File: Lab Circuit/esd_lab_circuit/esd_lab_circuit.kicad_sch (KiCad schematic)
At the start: 5 parts, among them U3 74LS373, U5 ATF16V8Bxx-xxPU, U6 M48Z35

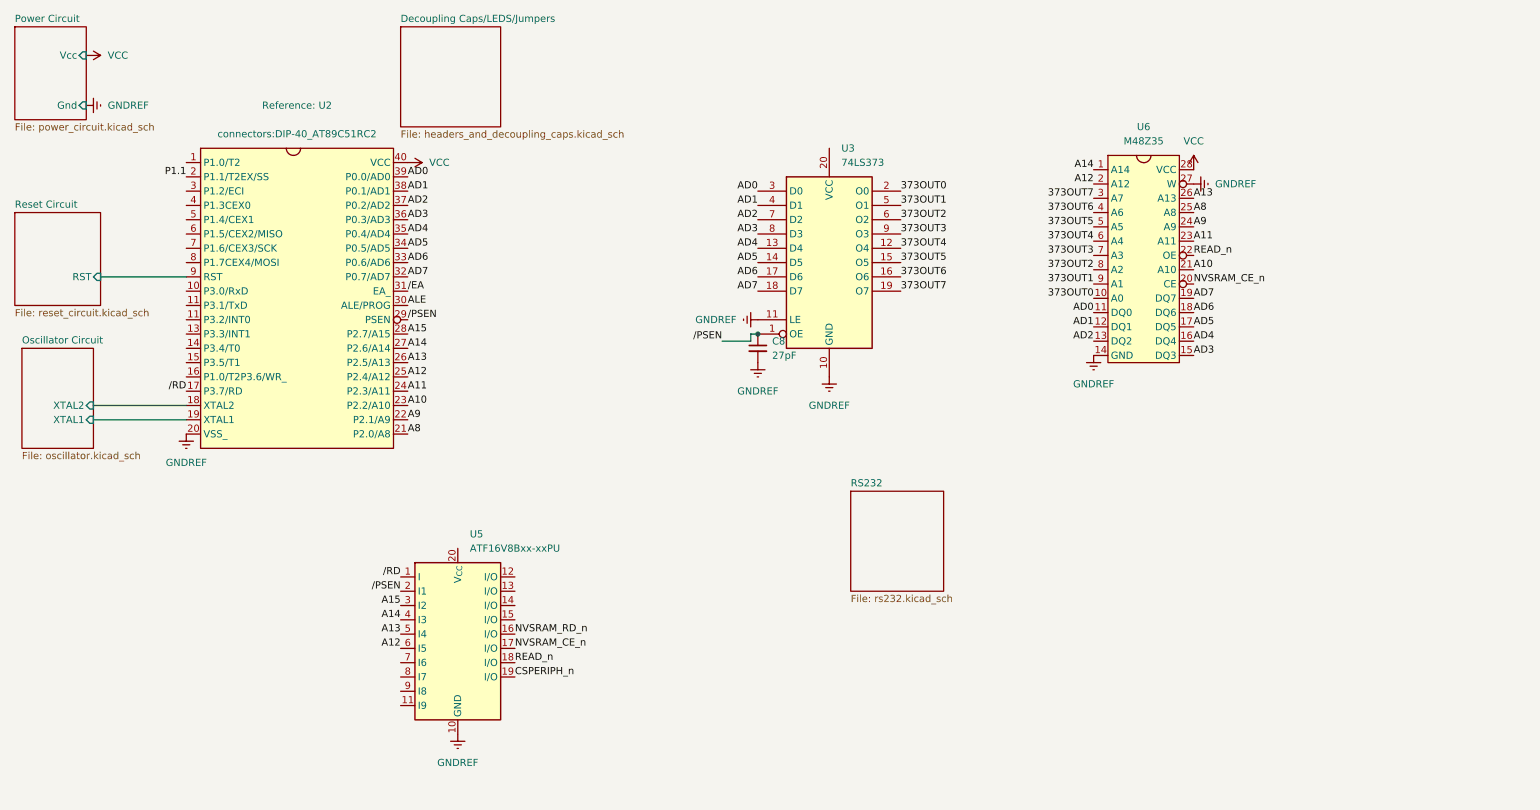
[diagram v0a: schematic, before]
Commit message: Added Debug Latch to schematic
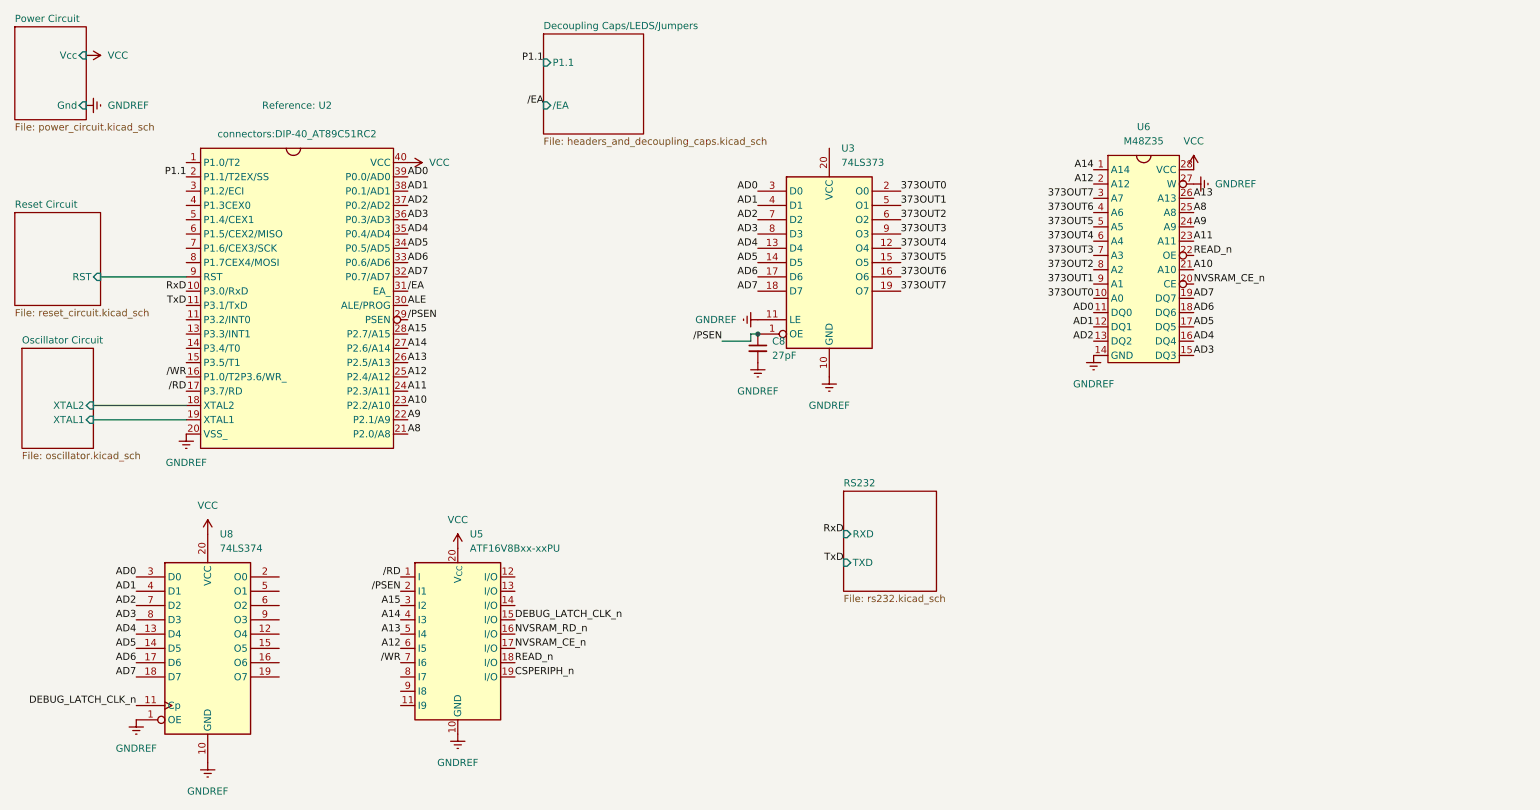
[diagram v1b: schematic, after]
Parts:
- added U8: 74LS374, symbol ESD:74LS374
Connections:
- net AD0: now also U8.3 (D0)
- net AD1: now also U8.4 (D1)
- net AD2: now also U8.7 (D2)
- net AD3: now also U8.8 (D3)
- net AD4: now also U8.13 (D4)
- net AD5: now also U8.14 (D5)
- net AD6: now also U8.17 (D6)
- net AD7: now also U8.18 (D7)
- net GNDREF: now also U8.1 (OE), U8.10 (GND)
- net VCC: now also U5.20 (V_{CC}), U8.20 (VCC)
- net DEBUG_LATCH_CLK_n: now reaches U5.15 (I/O)
- net DEBUG_LATCH_CLK_n: now also U8.11 (Cp)
- net /WR: now reaches U5.7 (I6)
- net /WR: now also U2.16 (P1.0/T2P3.6/WR_)
- net RxD: now reaches U2.10 (P3.0/RxD)
- net TxD: now reaches U2.11 (P3.2/INT0)
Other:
- sheet Decoupling Caps/LEDS/Jumpers ports: added P1.1, /EA; removed none
- sheet RS232 ports: added RXD, TXD; removed none

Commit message: Got to the point where lab 3 part 1 step 3 is done
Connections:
- net GNDREF: no longer U6.27 (W)
- net NVSRAM_WR_n: now reaches U5.14 (I/O)
- net NVSRAM_WR_n: now also U6.27 (W)
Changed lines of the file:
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@@
+		)
+	)
+	(label "NVSRAM_WR_n"
+		(at 102.87 118.11 0)
+		(effects
+			(font
+				(size 1.27 1.27)
+			)
+			(justify left bottom)
 		)
 	)
@@
 	(label "{slash}EA"
 		(at 83.82 62.23 0)
+		(effects
+			(font
+				(size 1.27 1.27)
+			)
+			(justify left bottom)
+		)
+	)
+	(label "NVSRAM_WR_n"
+		(at 223.52 43.18 0)
 		(effects
 			(font
@@
 					(unit 1)
 				)
-			)
-		)
-	)
-	(symbol
-		(lib_id "power:GNDREF")
-		(at 223.52 43.18 90)
-		(unit 1)
-		(exclude_from_sim no)
-		(in_bom yes)
-		(on_board yes)
-		(dnp no)
-		(fields_autoplaced yes)
-		(property "Reference" "#PWR019"
-			(at 229.87 43.18 0)
-			(effects
-				(font
-					(size 1.27 1.27)
-				)
-				(hide yes)
-			)
-		)
-		(property "Value" "GNDREF"
-			(at 227.33 43.1799 90)
-			(effects
-				(font
-					(size 1.27 1.27)
-				)
-				(justify right)
-			)
-		)
-		(property "Footprint" ""
-			(at 223.52 43.18 0)
-			(effects
-				(font
-					(size 1.27 1.27)
-				)
-				(hide yes)
-			)
-		)
-		(property "Datasheet" ""
-			(at 223.52 43.18 0)
-			(effects
-				(font
-					(size 1.27 1.27)
-				)
-				(hide yes)
-			)
-		)
-		(property "Description" "Power symbol creates a global label with name \"GNDREF\" , reference supply ground"
-			(at 223.52 43.18 0)
-			(effects
-				(font
-					(size 1.27 1.27)
-				)
-				(hide yes)
-			)
-		)
-		(pin "1"
-		)
-		(instances
-			(project ""
-				(path "/e737370b-dddd-4d85-b455-d3366cc4c4a7"
-					(reference "#PWR019")
-					(unit 1)
-				)

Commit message: Did the thing!!
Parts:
- added U9: 24LC16, symbol ESD:24LC16
- U2: value ~ -> (none)
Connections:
- net GNDREF: now also U9.4 (GND), U9.7 (WP)
- net VCC: now also U9.8 (VCC)
